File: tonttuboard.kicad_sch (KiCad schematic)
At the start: 45 parts, among them U3 ICM-40609-D, U4 BMP388, U5 W25Q256JVFIQT, U6 MMC5983MA, U9 Teensy 4.0

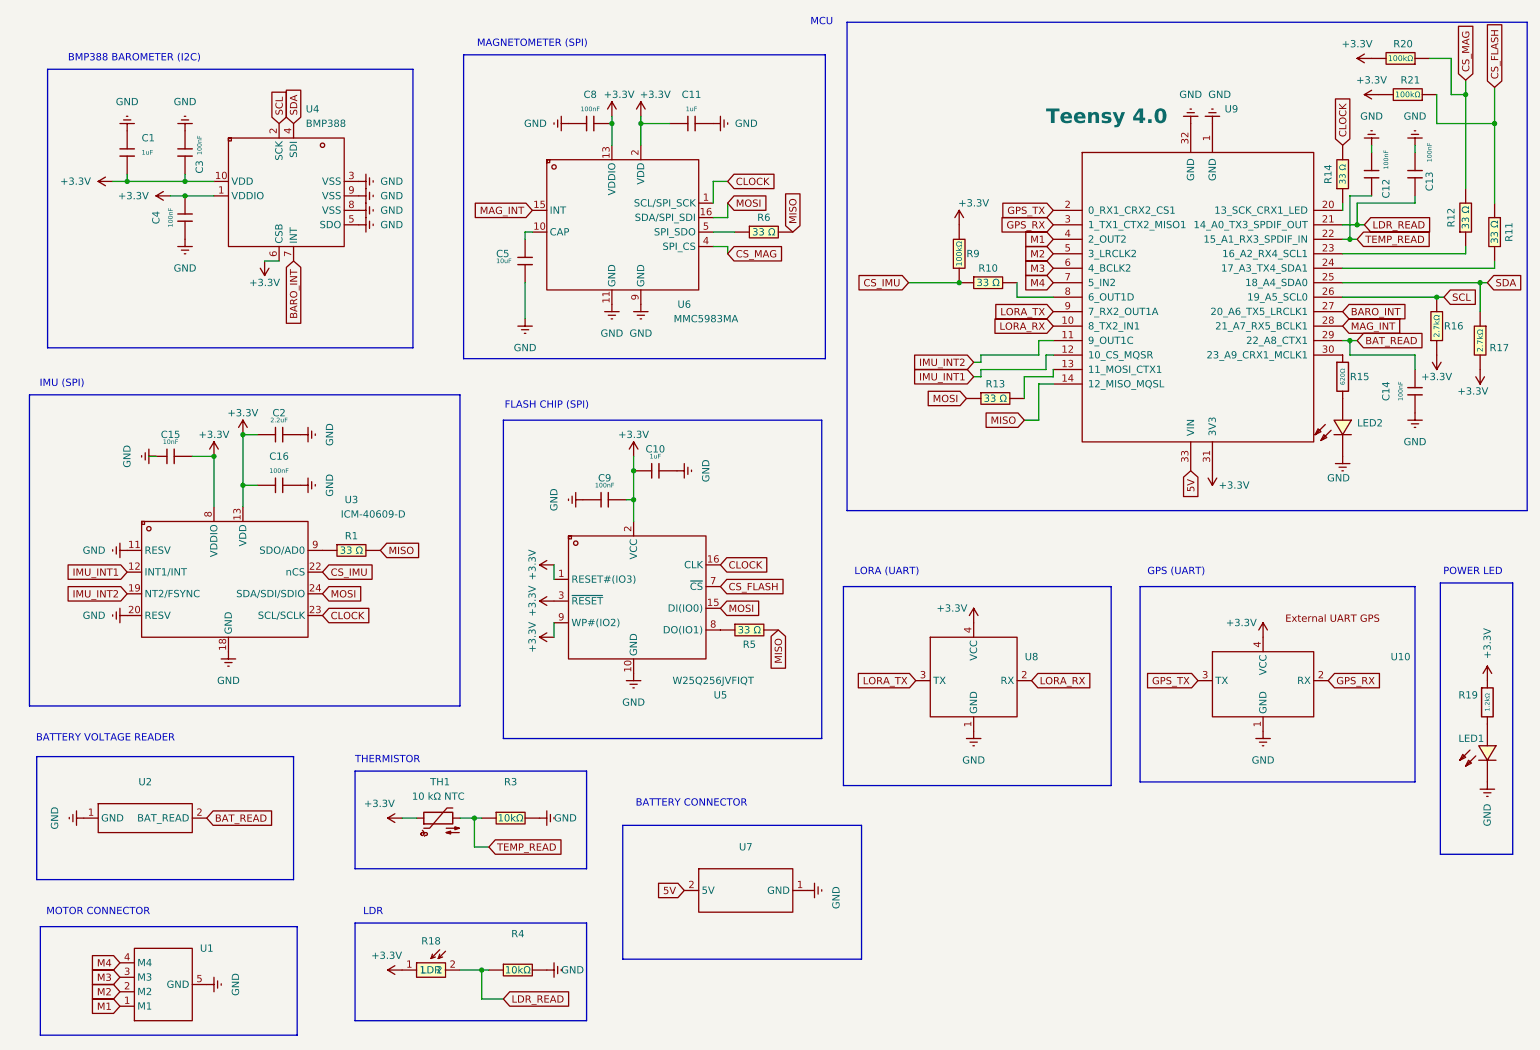
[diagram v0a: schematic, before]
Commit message: Improved component placement
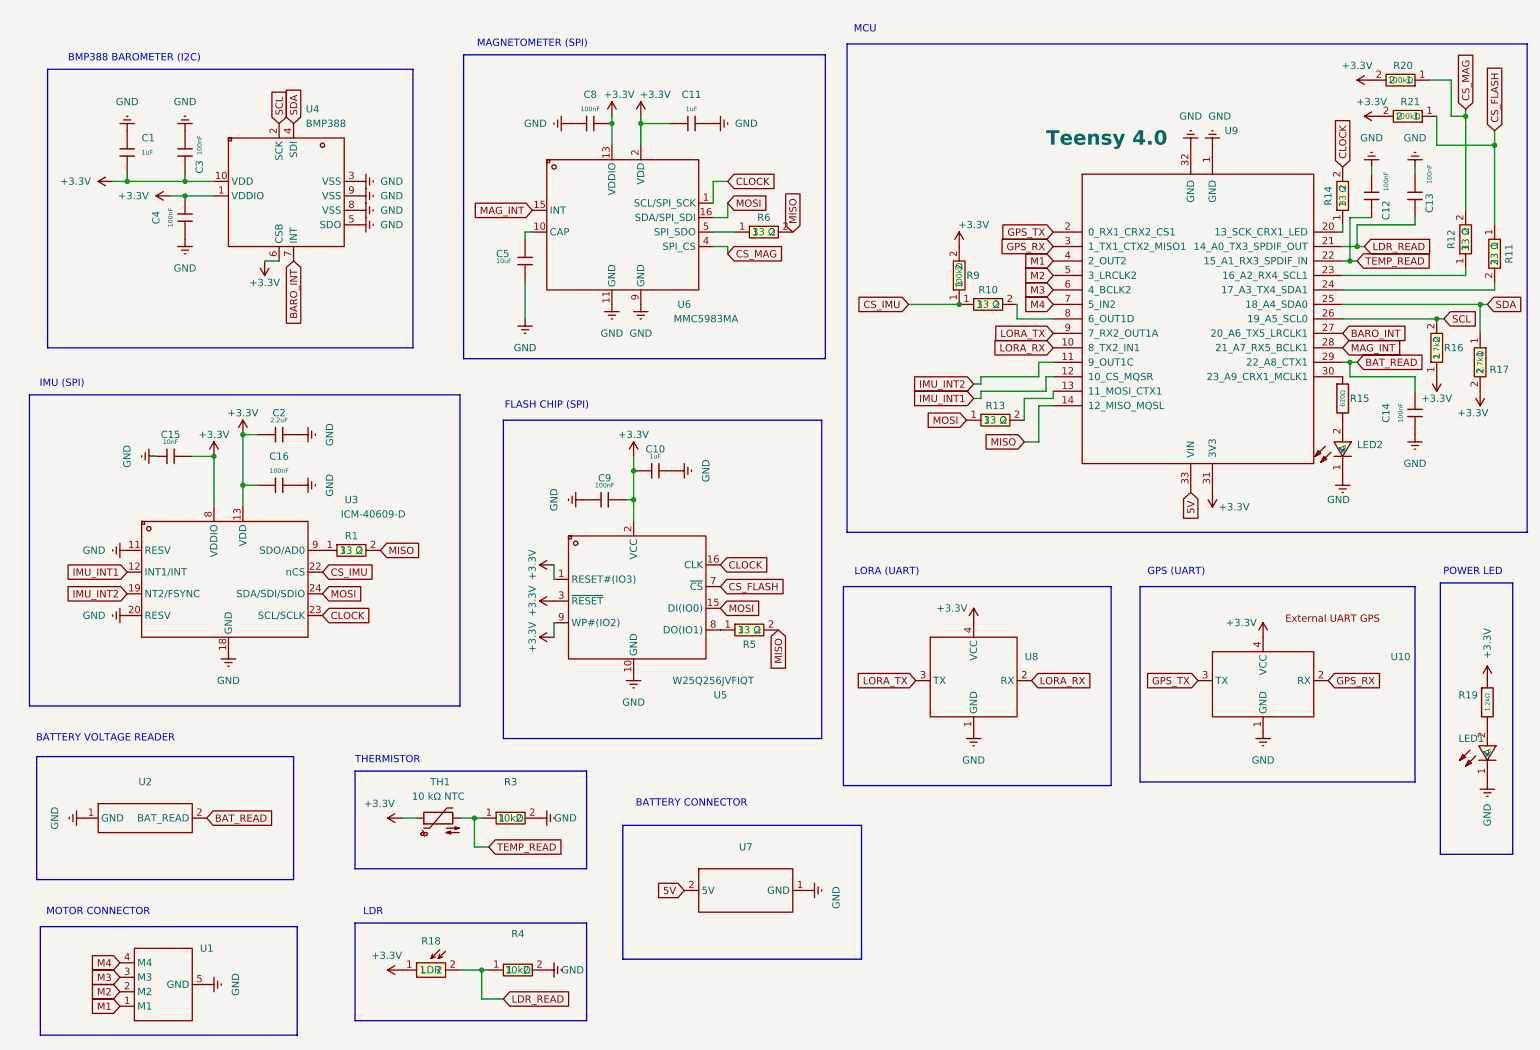
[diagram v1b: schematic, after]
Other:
- moved on the sheet: C12, C13, C14, R15, U9

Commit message: Added gnd vias and decorated
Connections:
- net CS_IMU: now also R12.2, R20.1; no longer R10.1, R9.1
- net CS_MAG: now also R10.1, R9.1; no longer R12.2, R20.1

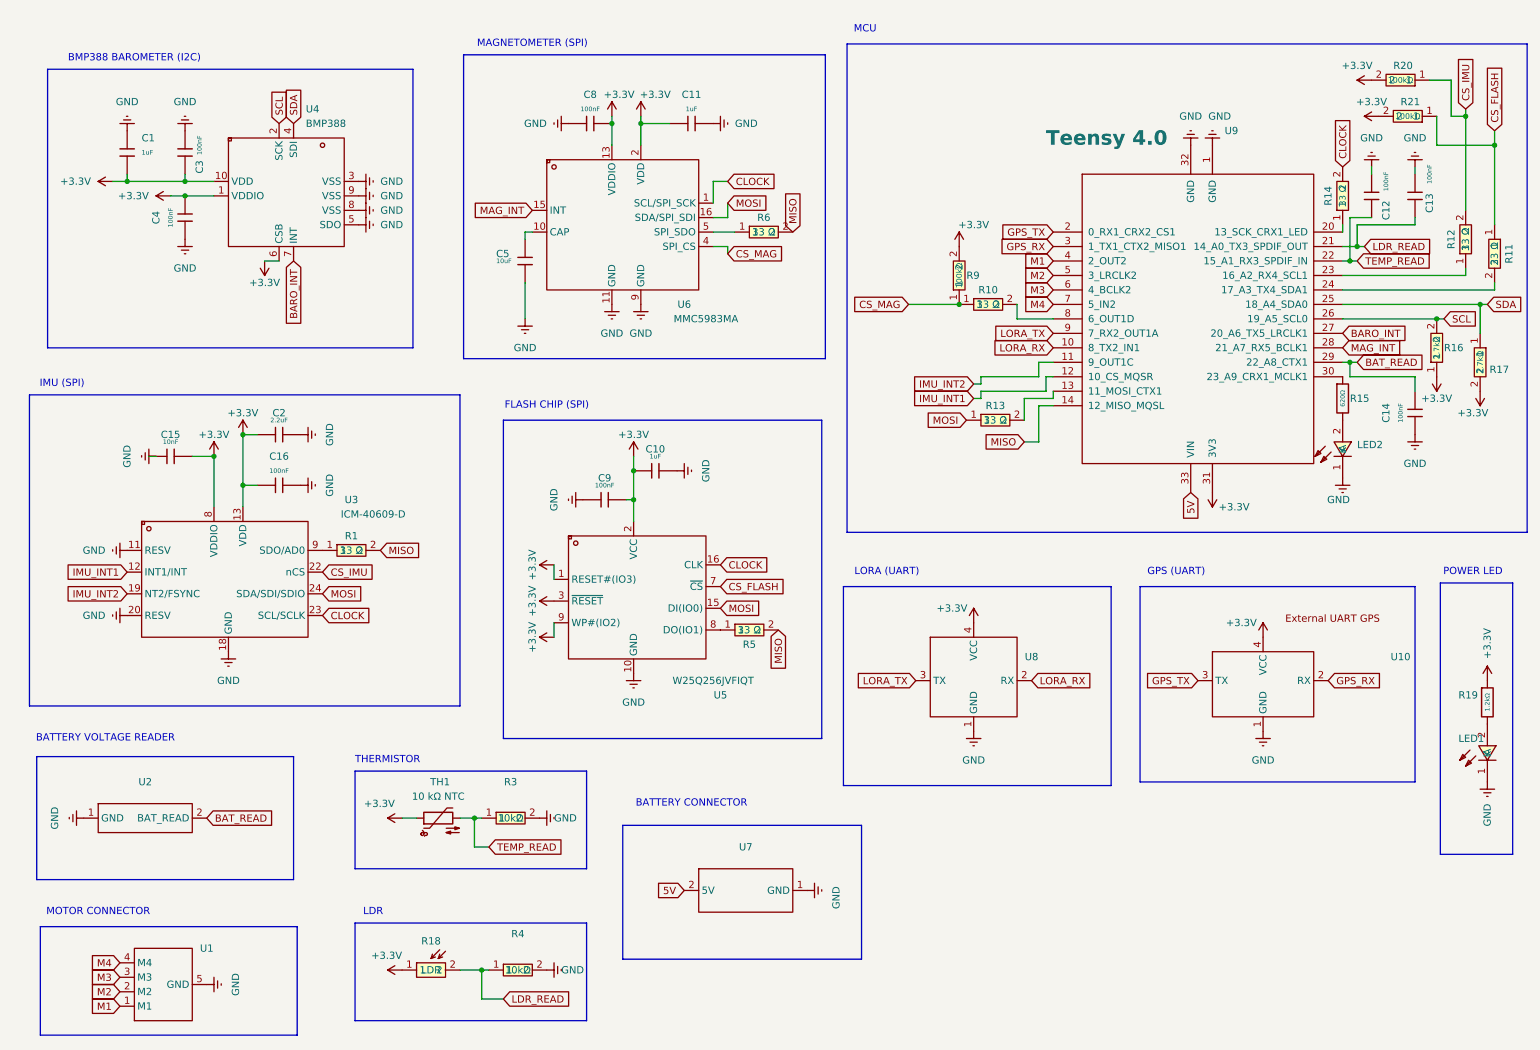
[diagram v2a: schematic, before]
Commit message: Replaced LDR with a through hole due to a soldering temperature issue. Also made the thermistor silk screen better and fixed a typo. Added CanSat 2026 Vaasa text to the back silkscreen
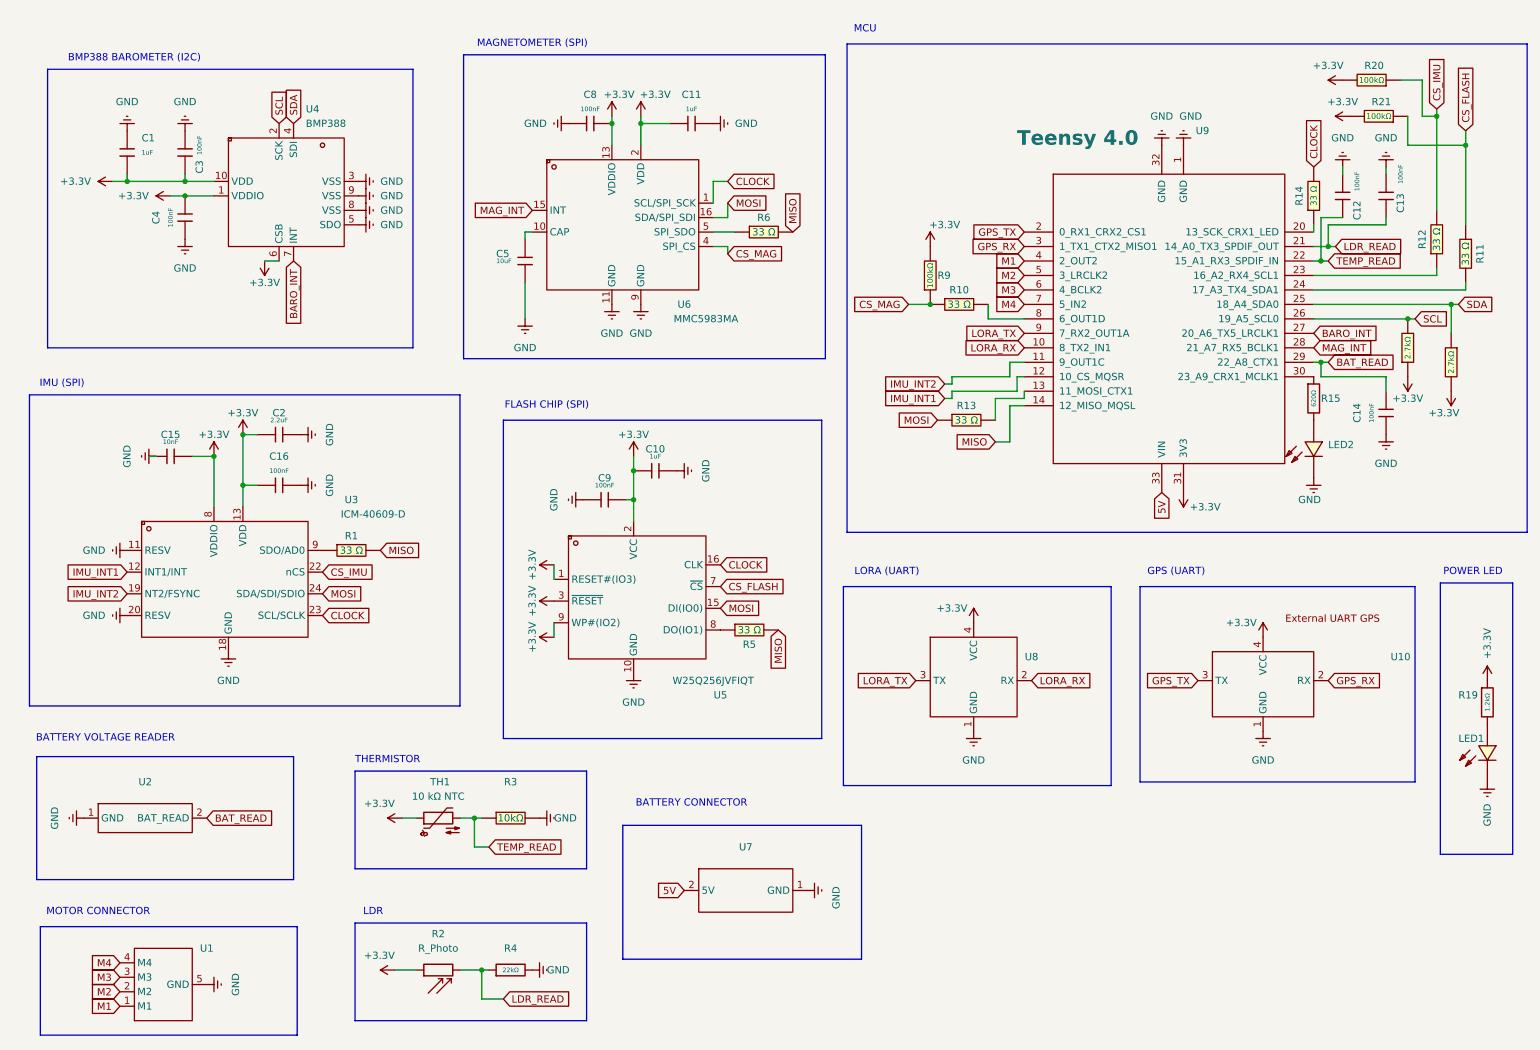
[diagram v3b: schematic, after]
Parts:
- removed R18: GT36516, EasyEDA:RES-SMD_L3.6-W2.4, symbol EasyEDA:GT36516
- removed R4: 0603WAF1002T5E, EasyEDA:R0603, symbol EasyEDA:0603WAF1002T5E
- added R2: R_Photo, Ossi connectors:LDR-holes, symbol Device:R_Photo
- added R4: 22kΩ, PCM_JLCPCB:R_0603, symbol PCM_JLCPCB-Resistors:0603,22kΩ
- TH1: footprint Ossi connectors:Thermisto-place -> Ossi connectors:Thermistor-holes
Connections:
- net +3.3V: now also R2.1
- net GND: now also R4.2
- net LDR_READ: now also R2.2, R4.1
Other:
- moved on the sheet: C12, C13, C14, R15, U9
